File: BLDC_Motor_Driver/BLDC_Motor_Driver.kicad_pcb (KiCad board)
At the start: 4 copper layers, 95 x 95 mm, 136 parts, among them J101 Conn_01x10, J102 395221002, J103 USB4105-GF-A, J104 Conn_01x05, J105 Conn_01x05, J106 Conn_01x04, J107 395221005, J108 395221003, J109 Conn_02x12_Counter_Clockwise, J110 395221005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

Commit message: most power routing done
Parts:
- J101: value Conn_01x10 -> Conn_01x08; footprint Connector_PinHeader_2.54mm:PinHeader_1x10_P2.54mm_Vertical -> Connector_PinHeader_2.54mm:PinHeader_1x08_P2.54mm_Vertical
- moved TP107 195.6 mm to (228.6, 131.1)
- moved SW101 9.08 mm to (203.3, 78.1)
- moved SW102 9.08 mm to (198.6, 78.1)
- moved R404 3.18 mm to (200.6, 118.8), turned to -90 degrees
- moved J101 2.54 mm to (204.3, 67.7)
- moved C412 1.55 mm to (226.7, 82.8)
- moved C414 1.55 mm to (221.6, 82.8)
- moved C415 1.55 mm to (216.6, 82.8)
- moved C416 1.50 mm to (216.6, 141.8)
- moved R416 1.50 mm to (216.6, 143.3)
- moved R412 1.45 mm to (226.7, 81.3)
- moved R414 1.45 mm to (221.6, 81.3)
- moved R415 1.45 mm to (216.6, 81.3)
- moved C201 0.80 mm to (200.9, 98.7)
- moved C207 0.80 mm to (200.9, 97.2)
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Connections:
- J101 pad 2: /Gate-Driver/ENC_B -> /Gate-Driver/GPIO0
- J101 pad 3: /Gate-Driver/ENC_N -> /Gate-Driver/GPIO1
- J101 pad 4: /Gate-Driver/GPIO0 -> /Gate-Driver/GPIO5
- J101 pad 5: /Gate-Driver/GPIO1 -> /Gate-Driver/GPIO15
- J101 pad 6: /Gate-Driver/GPIO5 -> /Gate-Driver/GPIO16
- J101 pad 7: /Gate-Driver/GPIO15 -> /Gate-Driver/GPIO17
- J101 pad 8: /Gate-Driver/GPIO16 -> /Gate-Driver/GPIO18
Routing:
- net +36V: track 6.05 -> 90.0 mm, vias 0 -> 26
- net /MOTOR_U: track 2.97 -> 37.8 mm
- net /5V_DRV: track 3.35 -> 35.0 mm, vias 0 -> 8
- net /MOTOR_W: track 4.25 -> 29.5 mm
- net /MOTOR_V: track 4.24 -> 25.2 mm
- net +3V3: track 2.33 -> 5.10 mm, vias 0 -> 18
- net Net-(D401-A): track 0.00 -> 1.56 mm
- net /DRIVER_FAULTN: track 28.7 -> 30.2 mm
- net /HALL_W_CONN: track 6.15 -> 5.10 mm
- net GND: vias 19 -> 71
- added copper zone on In2.Cu, net +36V
- added copper zone on F.Cu, net +3V3
- added copper zone on In2.Cu, net +3V3
- added copper zone on In2.Cu, net /5V_DRV
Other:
- board text added: "5V DRV"

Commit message: finished Gate Driver layout. remaining: MCU
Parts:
- moved J101 61.6 mm to (232.6, 122.5), turned to 0 degrees
- moved TP107 13.6 mm to (232.6, 144.1)
- moved J105 1.33 mm to (210.7, 96.2)
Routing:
- net /SPI2_SCK: track 0.00 -> 47.3 mm, vias 0 -> 2
- net /DRIVER_CS: track 0.00 -> 47.1 mm
- net /SPI2_MISO: track 0.00 -> 42.0 mm, vias 0 -> 2
- net /SPI2_MOSI: track 0.00 -> 40.0 mm, vias 0 -> 2
- net /Gate-Driver/GPIO18: track 0.00 -> 37.6 mm, vias 0 -> 1
- net /Gate-Driver/GPIO17: track 0.00 -> 35.4 mm, vias 0 -> 1
- net /Gate-Driver/GPIO16: track 0.00 -> 34.5 mm, vias 0 -> 1
- net /Gate-Driver/GPIO15: track 0.00 -> 30.2 mm, vias 0 -> 1
- net /Gate-Driver/GPIO5: track 0.00 -> 27.8 mm, vias 0 -> 1
- net /Gate-Driver/GPIO1: track 0.00 -> 24.4 mm, vias 0 -> 1
- net /Gate-Driver/GPIO0: track 0.00 -> 22.5 mm, vias 0 -> 1
- net /Gate-Driver/ENC_A/TXEN: track 33.5 -> 43.8 mm
- net +3V3: track 5.10 -> 8.26 mm, vias 18 -> 20
- net /5V_DRV: track 35.0 -> 38.0 mm, vias 8 -> 9
- net GND: vias 71 -> 68

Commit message: finsihed first draft. DRC errors remaining
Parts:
- moved TP101 187.7 mm to (216.1, 125.5)
- moved TP102 182.1 mm to (212.1, 125.5)
- moved TP113 178.7 mm to (216.1, 129.5)
- moved TP112 174.6 mm to (208.1, 129.5)
- moved TP110 174.2 mm to (212.1, 129.5)
- moved TP111 174.0 mm to (204.1, 129.5)
- moved TP108 173.2 mm to (208.1, 125.5)
- moved TP109 167.6 mm to (204.1, 125.5)
- moved C104 92.3 mm to (200.3, 84.9), turned to 0 degrees
- moved C102 84.0 mm to (205.0, 84.9), turned to 0 degrees
- moved R107 79.9 mm to (205.0, 86.3)
- moved D101 66.9 mm to (197.6, 89.4), turned to 180 degrees
- moved D102 66.9 mm to (197.6, 91.2), turned to 180 degrees
- moved D104 66.9 mm to (197.6, 94.9), turned to 180 degrees
- moved D103 66.9 mm to (197.6, 93.1), turned to 180 degrees
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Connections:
- J109 pad 10: /I2C2_SDA -> /USART2_TX
- J109 pad 11: /PC14 -> /SPI1_MOSI
- J109 pad 12: /I2C3_SCL -> /SPI1_MISO
- J109 pad 13: /PC15 -> unconnected-(J109-Pin_13-Pad13)
- J109 pad 14: /I2C3_SDA -> /SPI1_SCK
- J109 pad 15: /USART2_RX -> /I2C2_SDA
- J109 pad 16: /SPI1_MOSI -> /I2C2_SCL
- J109 pad 17: /USART2_TX -> /I2C1_SDA
- J109 pad 18: /SPI1_MISO -> /I2C1_SCL
- J109 pad 19: unconnected-(J109-Pin_19-Pad19) -> /I2C3_SDA
- J109 pad 20: /SPI1_SCK -> /I2C3_SCL
- J109 pad 3: /PA0 -> /PC13
- J109 pad 4: /I2C1_SCL -> /PC14
- J109 pad 5: /PA8 -> /PC15
- J109 pad 6: /I2C1_SDA -> /PA0
- J109 pad 8: /I2C2_SCL -> /PA8
- J109 pad 9: /PC13 -> /USART2_RX
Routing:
- net /PC13: track 0.00 -> 47.2 mm
- net /PC15: track 0.00 -> 43.6 mm
- net /PC14: track 0.00 -> 42.4 mm
- net /PA8: track 0.00 -> 39.7 mm
- net /NRST: track 0.00 -> 39.2 mm, vias 0 -> 2
- net /SPI1_MOSI: track 0.00 -> 38.1 mm, vias 0 -> 1
- net /BOOT0: track 0.00 -> 37.7 mm, vias 0 -> 2
- net /PA0: track 0.00 -> 36.2 mm
- net +1V8: track 3.02 -> 39.1 mm, vias 0 -> 2
- net /USART2_TX: track 0.00 -> 31.3 mm
- net /USART2_RX: track 0.00 -> 31.1 mm
- net /PB2: track 0.00 -> 31.1 mm
- net /SPI1_SCK: track 0.00 -> 29.4 mm, vias 0 -> 1
- net /I2C3_SDA: track 0.00 -> 29.2 mm, vias 0 -> 1
- net /I2C1_SDA: track 0.00 -> 25.0 mm
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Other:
- board text removed: "Status LEDs"

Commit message: clean layout done. signoff required
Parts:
- added NT1: NetTie_2, NetTie:NetTie-2_THT_Pad0.3mm, F.Cu at (245.2, 72.9)
- added NT2: NetTie_2, NetTie:NetTie-2_THT_Pad0.3mm, F.Cu at (242.6, 89.7)
- added NT3: NetTie_2, NetTie:NetTie-2_THT_Pad0.3mm, F.Cu at (239.2, 113.5)
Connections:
- U401 pad 35: GND -> /Gate-Driver/CSN_W
- U401 pad 46: GND -> /Gate-Driver/CSN_V
- U401 pad 47: GND -> /Gate-Driver/CSN_U
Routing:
- net /Gate-Driver/CSN_U: track 0.00 -> 51.1 mm, vias 0 -> 1
- net /Gate-Driver/CSN_V: track 0.00 -> 35.1 mm, vias 0 -> 1
- net /Gate-Driver/CSN_W: track 0.00 -> 17.4 mm, vias 0 -> 1
- net /Gate-Driver/CSP_U: track 44.9 -> 61.5 mm
- net /Gate-Driver/CSP_V: track 31.1 -> 47.3 mm
- net /Gate-Driver/HS_U: track 41.6 -> 54.2 mm
- net GND: track 7.33 -> 14.1 mm, vias 75 -> 68
- net /SPI2_SCK: track 47.3 -> 53.8 mm
- net /Gate-Driver/CSP_W: track 25.1 -> 22.9 mm
- net /SPI2_MISO: track 42.0 -> 43.9 mm
- net /Gate-Driver/LS_W: track 25.3 -> 26.6 mm
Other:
- outline, holes or cut-outs redrawn
- board text added: "!!HIGH POWER!!"
- board text added: "+36V"
- board text added: "1V8"
- board text added: "3V3"
- board text added: "5V_COMM"
- board text added: "5V_DRV"
- board text added: "5V_REG"
- board text added: "DRIVER_CS"
- board text added: "ENC_A"
- board text added: "ENC_A / TXEN"
- board text added: "ENC_B"
- board text added: "ENC_N"
- board text added: "EN_DRV"
- board text added: "GND"
- board text added: "GND 3V3"
- board text added: "GND TX RX 3V3"
- board text added: "GPIO_0"
- board text added: "GPIO_1"
- board text added: "GPIO_15"
- board text added: "GPIO_16"
- board text added: "GPIO_17"
- board text added: "GPIO_18"
- board text added: "GPIO_5"
- board text added: "HALL_U"
- board text added: "HALL_V"
- board text added: "HALL_W"
- board text added: "I2C1"
- board text added: "I2C2"
- board text added: "I2C3"
- board text added: "MISO"
- board text added: "MOSI"
- board text added: "MOTOR_U"
- board text added: "MOTOR_V"
- board text added: "MOTOR_W"
- board text added: "NRST"
- board text added: "PB2 PA8"
- board text added: "PC13 PC14"
- board text added: "PC15 PA0"
- board text added: "SCK"
- board text added: "SPI1_MOSI MISO"
- board text added: "SPI1_SCK"
- board text added: "SWCLK"
- board text added: "SWDIO"
- board text added: "TP101"
- board text added: "TP102"
- board text added: "TP107"
- board text added: "TP108"
- board text added: "TP109"
- board text added: "TP110"
- board text added: "TP111"
- board text added: "TP112"
- board text added: "TP113"
- board text added: "UART2_RX TX"
- board text added: "VBUCK"
- board text added: "V_EXT2"
- board text removed: "+36 -> +5"
- board text removed: "3V3 RX TX GND"
- board text removed: "5V DRV"
- board text removed: "DRV"
- board text removed: "EN"
- board text removed: "Gate Driver (G_DRV) Area"
- board text removed: "Kelvin Connection: must be parallel to G_DRV"
- board text removed: "MCU Area"
- board text removed: "USB_PWR"
- board text removed: "User LEDs"

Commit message: resolved all but DRC warning
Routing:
- net /SPI2_SCK: track 53.8 -> 51.0 mm
- net /SPI2_MISO: track 43.9 -> 42.0 mm
- net GND: vias 68 -> 77
- net +3V3: vias 24 -> 25
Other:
- board text added: "Noah B"
- board text added: "SPRING 2026 ECE 395"
- board text added: "Thomas M"

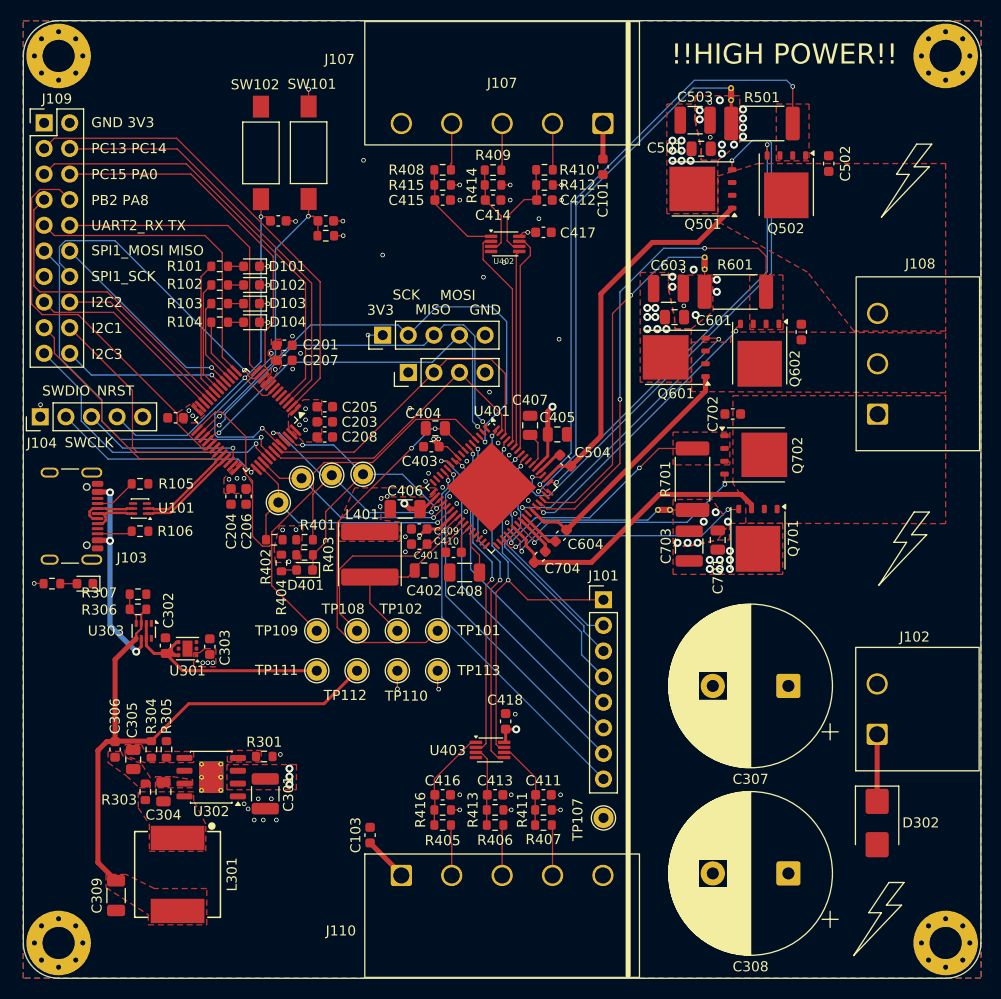
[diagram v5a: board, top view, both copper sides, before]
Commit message: fixed drc issues, added gnd vias
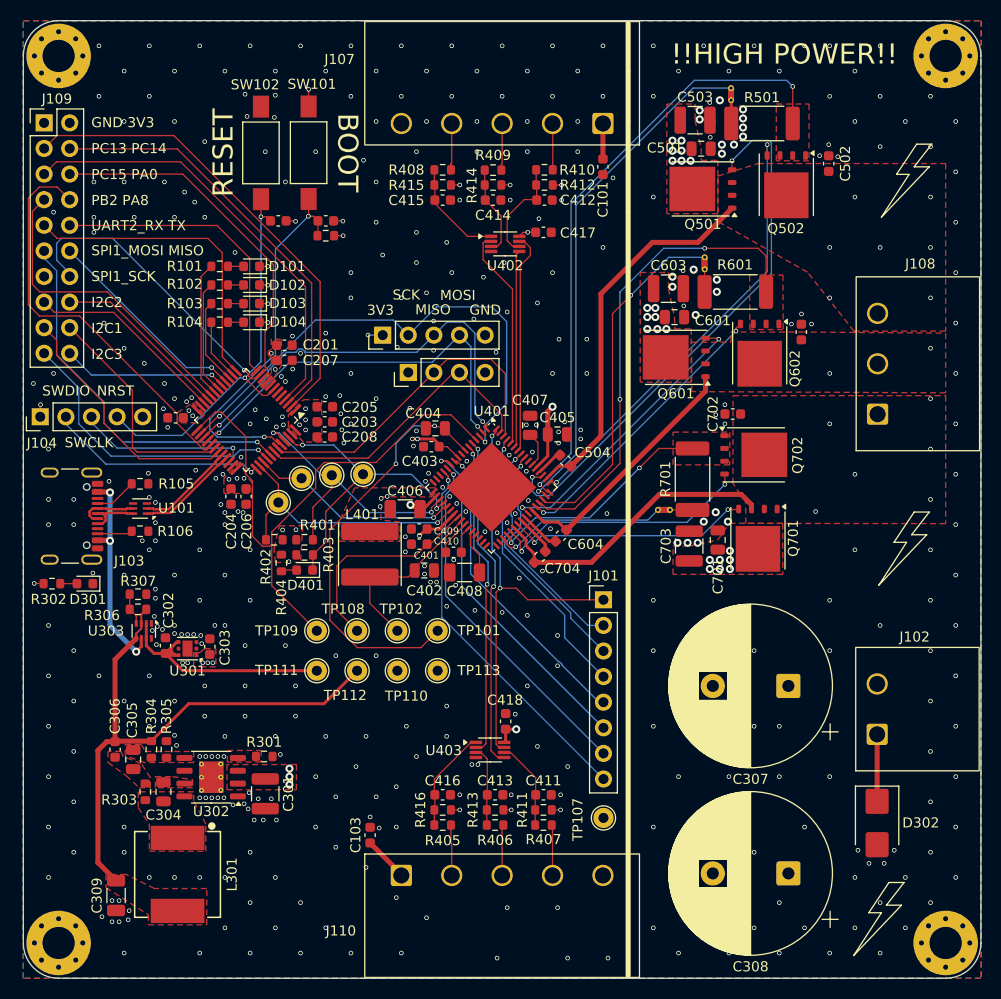
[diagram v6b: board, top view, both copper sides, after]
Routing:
- net /5V_DRV: track 38.0 -> 60.0 mm
- net +1V8: track 39.1 -> 41.5 mm
- net GND: track 14.1 -> 12.3 mm, vias 77 -> 468
- net +3V3: track 13.2 -> 11.7 mm, vias 25 -> 24
- net /PA8: track 39.7 -> 40.6 mm
- net /SPI1_SCK: track 29.4 -> 30.2 mm
- net /SPI2_MISO: track 42.0 -> 42.7 mm
- net +36V: track 90.0 -> 89.3 mm
- net /SPI1_MOSI: track 38.1 -> 37.4 mm
- net /USART2_TX: track 31.3 -> 30.7 mm
- net /DRIVER_V_{EXT2}: track 20.7 -> 21.3 mm
- net /DRIVER_FAULTN: track 30.2 -> 30.7 mm
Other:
- board text added: "BOOT"
- board text added: "RESET"
